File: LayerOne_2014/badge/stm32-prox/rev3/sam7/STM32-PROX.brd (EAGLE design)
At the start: 99 x 50 mm, 273 parts, among them IC10 74XX244, IC105 MCP1824T-250, IC106 MCP1824T-120, IC11 CD4066, IC12 AT91SAM7S64, IC13 PQ1X331M2ZP-3V3-LDO-SOT-23-5, IC14 AD8052, IC3 PQ1X331M2ZP-3V3-LDO-SOT-23-5, IC4 HCU-INVERTER, IC5 TLV3502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

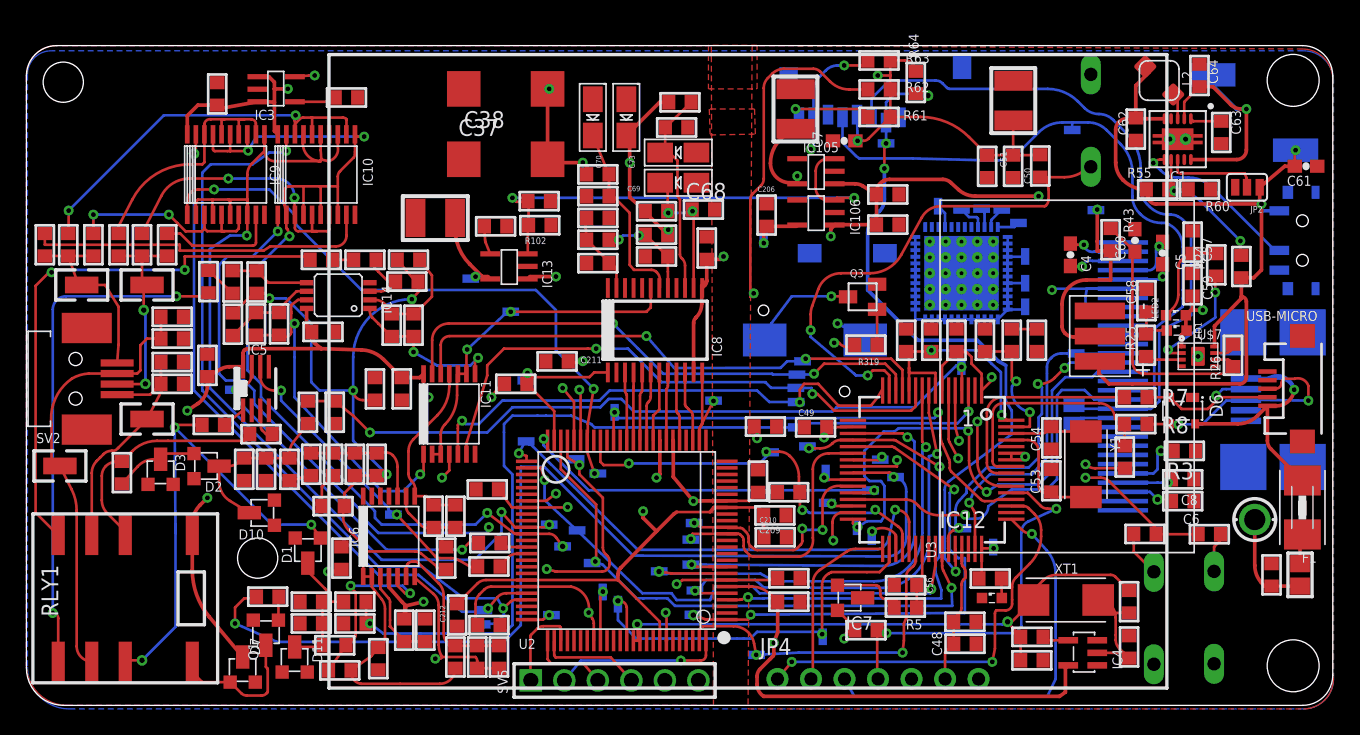
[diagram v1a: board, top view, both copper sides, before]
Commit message: speaker changed.
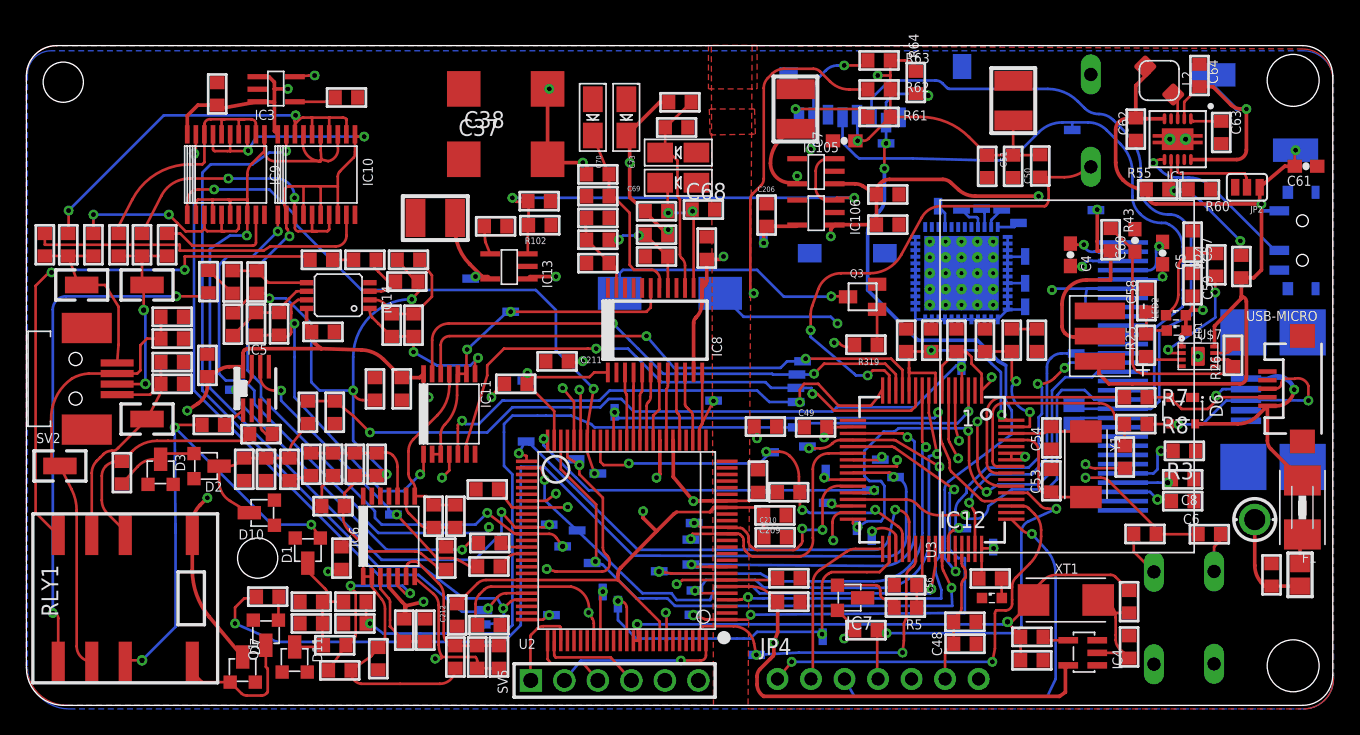
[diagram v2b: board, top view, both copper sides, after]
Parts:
- moved BUZ1 11.5 mm to (48.8, 30.2)
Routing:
- net N$59: track 8.21 -> 19.8 mm
- net +3V3: track 243.6 -> 251.0 mm
- added copper zone on layer 2, net GND
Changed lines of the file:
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@@
 <setting verticaltext="up"/>
 </settings>
-<grid distance="10" unitdist="mil" unit="mil" style="dots" multiple="1" display="yes" altdistance="0.0025" altunitdist="inch" altunit="inch"/>
+<grid distance="1" unitdist="mm" unit="mm" style="dots" multiple="1" display="yes" altdistance="0.1" altunitdist="mm" altunit="mm"/>
 <layers>
 <layer number="1" name="Top" color="4" fill="1" visible="yes" active="yes"/>
@@
 <layer number="19" name="Unrouted" color="6" fill="1" visible="yes" active="yes"/>
 <layer number="20" name="Dimension" color="15" fill="1" visible="yes" active="yes"/>
-<layer number="21" name="tPlace" color="7" fill="1" visible="yes" active="yes"/>
-<layer number="22" name="bPlace" color="7" fill="1" visible="yes" active="yes"/>
+<layer number="21" name="tPlace" color="7" fill="1" visible="no" active="yes"/>
+<layer number="22" name="bPlace" color="7" fill="1" visible="no" active="yes"/>
 <layer number="23" name="tOrigins" color="15" fill="1" visible="yes" active="yes"/>
 <layer number="24" name="bOrigins" color="15" fill="1" visible="yes" active="yes"/>
@@
 <layer number="43" name="vRestrict" color="2" fill="10" visible="no" active="yes"/>
 <layer number="44" name="Drills" color="7" fill="1" visible="no" active="yes"/>
-<layer number="45" name="Holes" color="7" fill="1" visible="yes" active="yes"/>
+<layer number="45" name="Holes" color="7" fill="1" visible="no" active="yes"/>
 <layer number="46" name="Milling" color="3" fill="1" visible="no" active="yes"/>
 <layer number="47" name="Measures" color="7" fill="1" visible="no" active="yes"/>
@@
 <wire x1="2.832684375" y1="-1" x2="96.714" y2="-1" width="0" layer="20"/>
 <wire x1="96.714" y1="-1" x2="99" y2="1.286" width="0" layer="20" curve="90"/>
-<text x="6.46551875" y="33.95144375" size="1.778" layer="52" rot="MR270">www.layerone.org</text>
-<text x="2.6445125" y="35.153565625" size="1.778" layer="52" rot="MR270">LayerOne 2014</text>
+<text x="7.46551875" y="32.95144375" size="1.778" layer="52" rot="MR270">www.layerone.org</text>
+<text x="2.6445125" y="31.153565625" size="1.778" layer="52" rot="MR270">LayerOne 2014</text>
 <text x="23.161175" y="2.4405875" size="1.778" layer="52" rot="MR180">charliex</text>
 <text x="13.843" y="40.64" size="1.778" layer="52" rot="MR270">[ NULL SPACE LABS ]</text>
@@
 arko
 krs</text>
-<text x="48.514" y="41.656" size="1.778" layer="52" rot="MR270">Ten Year Anniversary</text>
+<text x="30.514" y="41.656" size="1.778" layer="52" rot="MR270">Ten Year Anniversary</text>
 <wire x1="74.12868125" y1="-0.2264875" x2="74.12868125" y2="-0.2076125" width="0.4064" layer="52"/>
 <wire x1="77.93868125" y1="-0.2264875" x2="77.93868125" y2="-0.2076125" width="0.4064" layer="52"/>
@@
 <element name="SV1" library="STM32-PROX" package="USB-MINIB-SMD" value="USB-MINIB" x="94.4245" y="23.368" smashed="yes" rot="MR0">
 <attribute name="PARTNO" value="*" x="94.4245" y="23.368" size="1.778" layer="28" rot="MR0" display="off"/>
-<attribute name="NAME" x="88.73055625" y="16.3388" size="1.27" layer="22" ratio="18" rot="MR90"/>
+<attribute name="NAME" x="97.7072" y="13.54655625" size="1.27" layer="22" ratio="18" rot="MR0"/>
 <attribute name="OC_NEWARK" value="unknown" x="94.4245" y="23.368" size="1.778" layer="28" rot="MR0" display="off"/>
 <attribute name="MF" value="" x="94.4245" y="23.368" size="1.778" layer="28" rot="MR0" display="off"/>
@@
 <element name="K3" library="STM32-PROX" package="B3F-5XX" value="" x="90.037" y="5.651" smashed="yes" rot="MR90">
 <attribute name="PARTNO" value="PTS635SL50 LFS" x="90.037" y="5.651" size="1.778" layer="28" rot="MR90" display="off"/>
-<attribute name="NAME" x="92.346903125" y="7.8504125" size="1.27" layer="26" ratio="10" rot="MR90"/>
+<attribute name="NAME" x="92.346903125" y="1.5004125" size="1.27" layer="26" ratio="10" rot="MR90"/>
 <attribute name="VALUE" x="86.457" y="2.603" size="1.27" layer="28" ratio="10" rot="MR90"/>
 <attribute name="OC_NEWARK" value="unknown" x="90.037" y="5.651" size="1.778" layer="28" rot="MR90" display="off"/>
@@
 <attribute name="DIGIKEY" value="MICROSMD050FCT-ND" x="96.7" y="14" size="1.778" layer="27" rot="R90" display="off"/>
 </element>
-<element name="BUZ1" library="STM32-PROX" package="BUZZER" value="BUZZER" x="59.76" y="26.69" smashed="yes" rot="MR180">
-<attribute name="NAME" x="61.30225625" y="34.58605625" size="0.8128" layer="26" ratio="10" rot="MR0"/>
-<attribute name="VALUE" x="61.36" y="31.79" size="0.8128" layer="28" ratio="10" rot="MR270"/>
-<attribute name="PARTNO" value="CCV-084B16" x="59.76" y="26.69" size="1.778" layer="28" rot="MR180" display="off"/>
-<attribute name="OC_NEWARK" value="unknown" x="59.76" y="26.69" size="1.778" layer="28" rot="MR180" display="off"/>
-<attribute name="MF" value="CCV-084B16" x="59.76" y="26.69" size="1.778" layer="28" rot="MR180" display="off"/>
-<attribute name="MPN" value="CCV-084B16" x="59.76" y="26.69" size="1.778" layer="28" rot="MR180" display="off"/>
-<attribute name="DIGIKEY" value="102-1265-1-ND" x="59.76" y="26.69" size="1.778" layer="28" rot="MR180" display="off"/>
-</element>
 <element name="R319" library="STM32-PROX" package="RLC_0603" value="100" x="63.623" y="26.336" smashed="yes" rot="R180">
 <attribute name="NAME" x="64.629684375" y="25.291021875" size="0.5" layer="25" font="vector" rot="R180"/>
@@
 <element name="TP44" library="STM32-PROX" package="SMD-TESTPOINT" value="TESTPAD" x="75.692" y="30.988" rot="MR90"/>
 <element name="TP56" library="STM32-PROX" package="SMD-TESTPOINT" value="TESTPAD" x="75.692" y="33.02" rot="MR90"/>
+<element name="BUZ1" library="STM32-PROX" package="BUZZER" value="BUZZER" x="48.768" y="30.226" rot="MR180"/>
 </elements>
 <signals>
@@
 <contactref element="U40" pad="2"/>
 <contactref element="U40" pad="3"/>
+<polygon width="0.4064" layer="2">
+<vertex x="0" y="48.768"/>
+<vertex x="99.06" y="48.768"/>
+<vertex x="99.06" y="-1.524"/>
+<vertex x="0" y="-1.524"/>
+</polygon>
 <wire x1="91.611" y1="38.263" x2="97.825" y2="39.859" width="0" layer="19" extent="1-1"/>
 <wire x1="89.75" y1="38.1" x2="91.611" y2="38.263" width="0" layer="19" extent="1-1"/>
@@
 <signal name="N$59">
 <contactref element="Q3" pad="3"/>
-<contactref element="BUZ1" pad="2"/>
-<wire x1="55.95" y1="26.69" x2="56.458" y2="27.95" width="0.2032" layer="16"/>
-<wire x1="56.458" y1="27.95" x2="58" y2="30" width="0.2032" layer="16"/>
-<wire x1="58" y1="30" x2="61" y2="30" width="0.2032" layer="16"/>
 <via x="61" y="30" extent="1-16" drill="0.3556"/>
 <wire x1="61" y1="30" x2="62.232" y2="30" width="0.2032" layer="1"/>
 <wire x1="62.232" y1="30" x2="62.269" y2="29.963" width="0.2032" layer="1"/>
+<contactref element="BUZ1" pad="2"/>
+<wire x1="44.958" y1="30.226" x2="44.958" y2="31.75" width="0.2032" layer="16"/>
+<wire x1="44.958" y1="31.75" x2="45.212" y2="32.004" width="0.2032" layer="16"/>
+<wire x1="45.212" y1="32.004" x2="55.372" y2="32.004" width="0.2032" layer="16"/>
+<wire x1="55.372" y1="32.004" x2="57.404" y2="29.972" width="0.2032" layer="16"/>
+<wire x1="57.404" y1="29.972" x2="60.972" y2="29.972" width="0.2032" layer="16"/>
+<wire x1="60.972" y1="29.972" x2="61" y2="30" width="0.2032" layer="16"/>
 </signal>
 <signal name="N$60">
@@
 <contactref element="C49" pad="1"/>
 <contactref element="C50" pad="1"/>
-<contactref element="BUZ1" pad="1"/>
 <contactref element="U3" pad="6"/>
 <contactref element="U3" pad="9"/>
@@
 <wire x1="71.247" y1="25.781" x2="70.524" y2="25.781" width="0.2032" layer="1"/>
 <wire x1="70.524" y1="25.781" x2="70.485" y2="25.82" width="0.2032" layer="1"/>
-<wire x1="63.57" y1="26.69" x2="63.336" y2="26.924" width="0.2032" layer="16" curve="90"/>
-<wire x1="63.336" y1="26.924" x2="61.468" y2="27.94" width="0.2032" layer="16"/>
 <via x="61.468" y="27.94" extent="3-16" drill="0.3556"/>
 <wire x1="61.468" y1="27.94" x2="70.104" y2="27.94" width="0.2032" layer="3"/>
@@
 <wire x1="60.657" y1="20.017" x2="60.657" y2="20.073" width="0.2032" layer="1"/>
 <wire x1="70.27" y1="5.5635" x2="70.27" y2="5.334" width="0.2032" layer="1"/>
+<contactref element="BUZ1" pad="1"/>
+<wire x1="52.578" y1="30.226" x2="54.356" y2="28.448" width="0.2032" layer="16"/>
+<wire x1="54.356" y1="28.448" x2="60.96" y2="28.448" width="0.2032" layer="16"/>
+<wire x1="60.96" y1="28.448" x2="61.468" y2="27.94" width="0.2032" layer="16"/>
 </signal>
 <signal name="USB_PU">

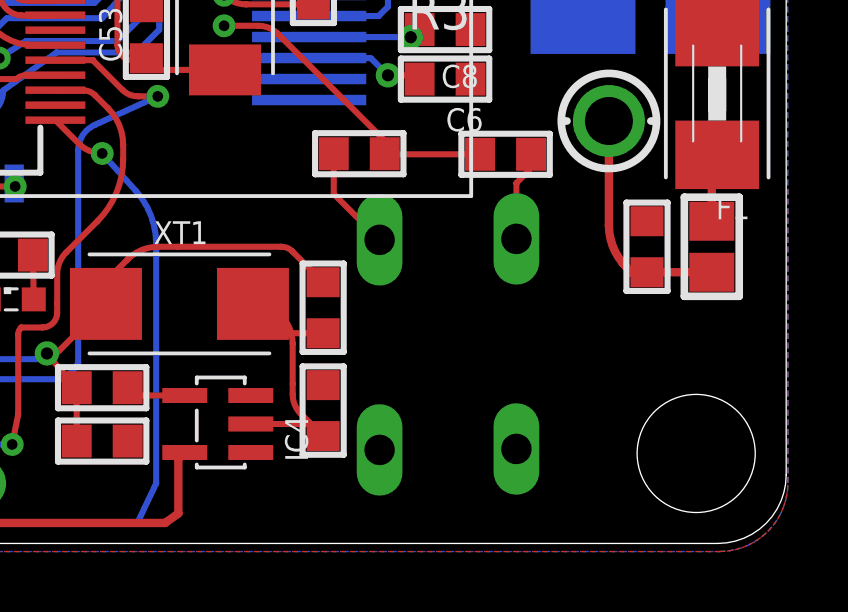
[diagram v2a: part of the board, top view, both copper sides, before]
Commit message: 
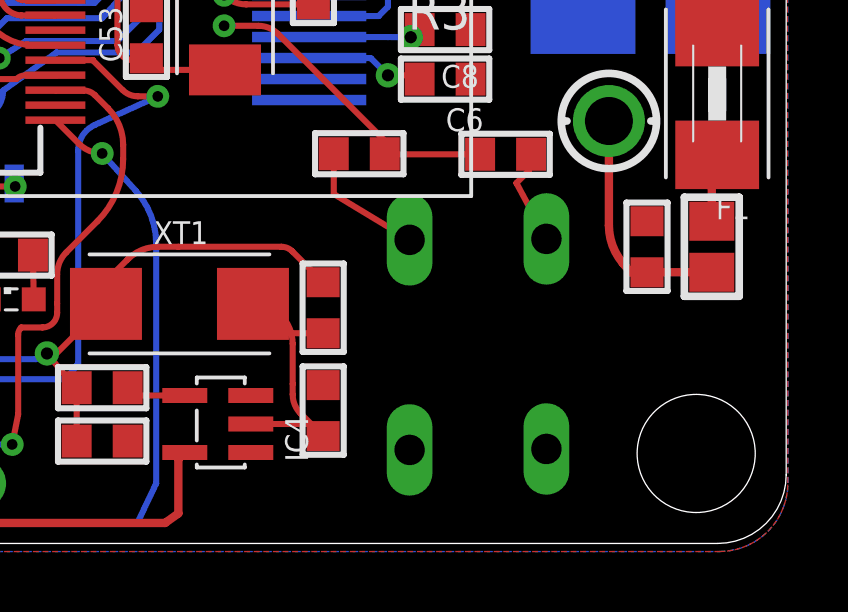
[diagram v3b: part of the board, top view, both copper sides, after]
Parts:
- moved K2 1.00 mm to (86.5, 5.62)
- moved K3 1.00 mm to (91.0, 5.65)
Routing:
- net SW_K2: track 29.1 -> 30.7 mm
- net SW_K3: track 30.5 -> 31.5 mm

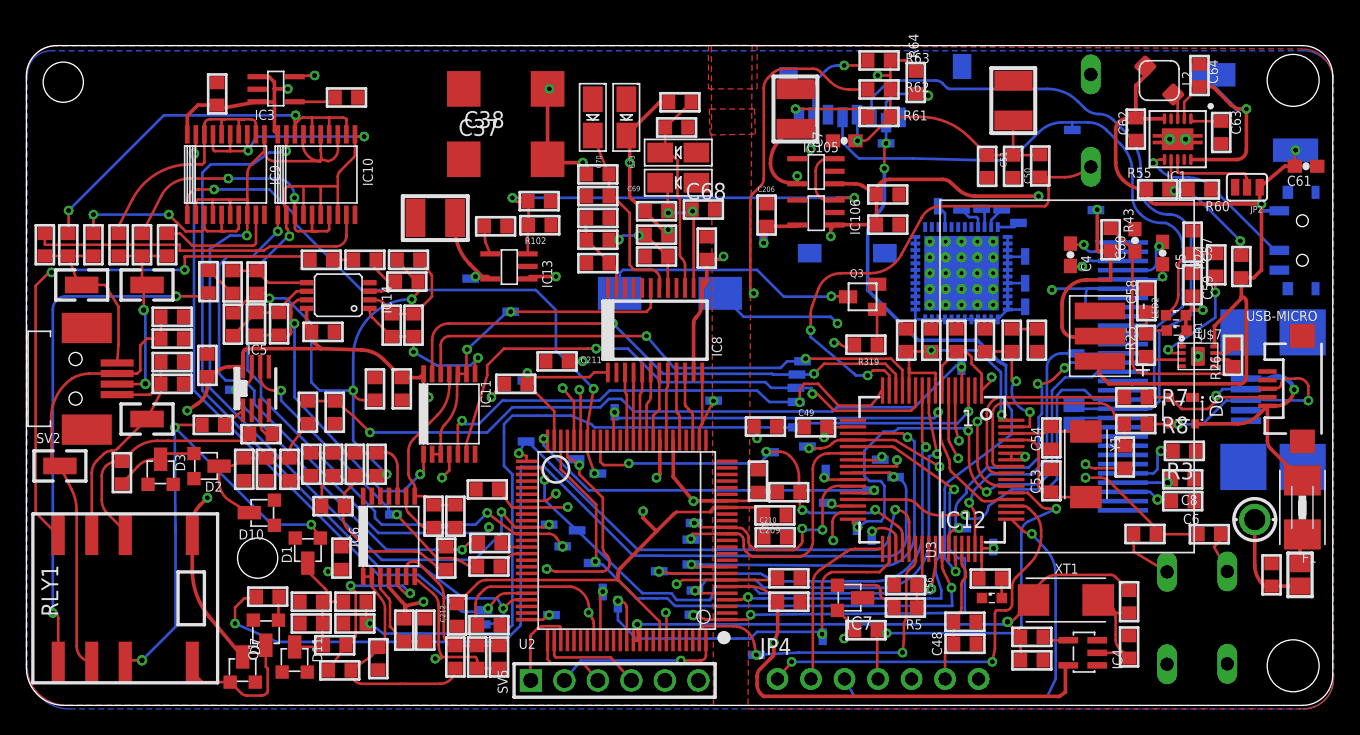
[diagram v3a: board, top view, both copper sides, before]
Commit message: switched on gnds
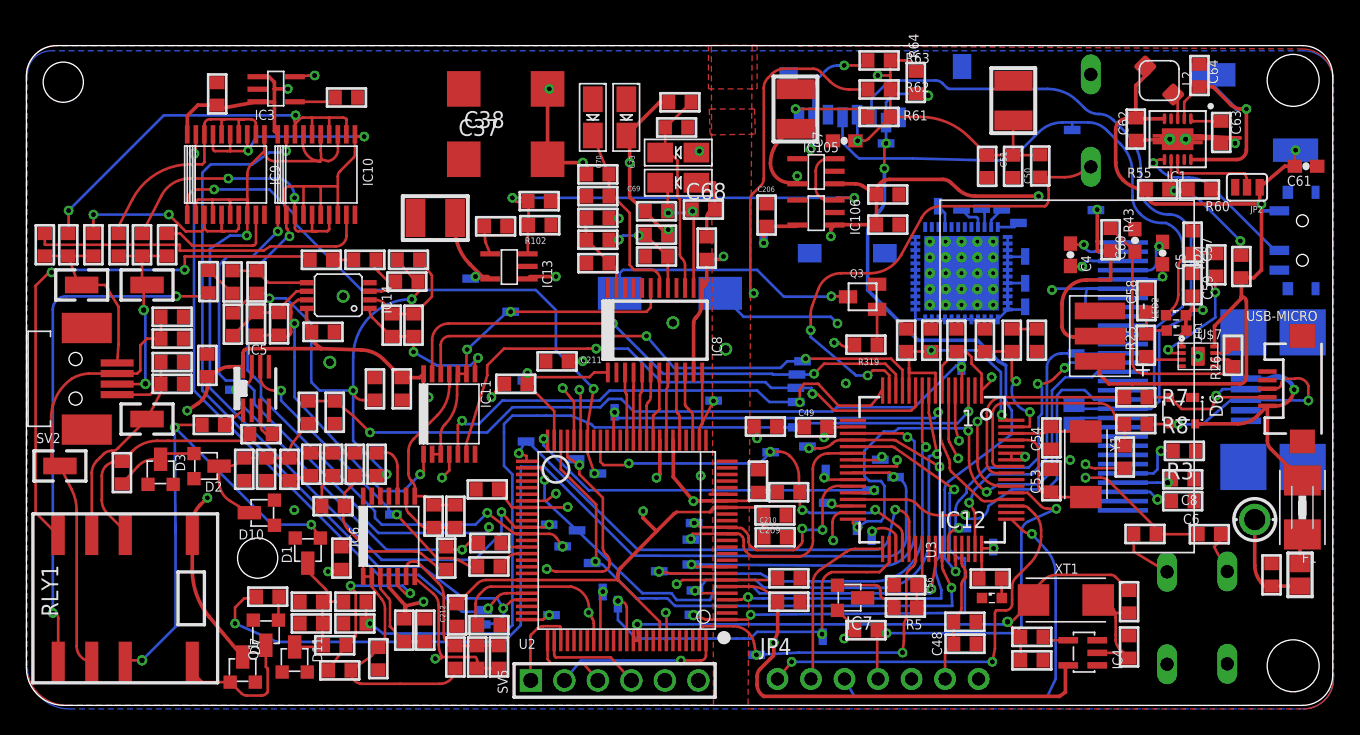
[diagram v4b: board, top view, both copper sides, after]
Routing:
- net GND: track 0.00 -> 17.6 mm, vias 0 -> 11
- net +2V5: track 93.4 -> 92.8 mm
- net FPGA_NINIT: track 31.7 -> 31.1 mm

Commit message: all gnds routed
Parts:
- moved R65 2.06 mm to (74.3, 10.3), turned to 270 degrees
- moved C56 2.03 mm to (66.6, 6.07)
- moved R5 1.40 mm to (66.6, 7.81)
- moved R4 1.02 mm to (63.6, 3.68)
- moved TP53 0.92 mm to (69.9, 24.6), turned to 180 degrees
- moved XT1 0.25 mm to (81.3, 6.99)
- moved C212 0.25 mm to (32.6, 6.10)
- turned R10 to 90 degrees
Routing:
- net GND: track 17.6 -> 52.3 mm, vias 11 -> 54
- net +3V3: track 251.0 -> 254.6 mm
- net SW_K1: track 38.8 -> 40.9 mm
- net N$69: track 5.77 -> 4.39 mm
- net N$76: track 40.5 -> 39.5 mm
- net AMPL_HI: track 55.2 -> 56.2 mm
- net LED3: track 1.48 -> 2.36 mm
- net JTAG_TMS: track 31.8 -> 32.6 mm
- net FPGA_NINIT: track 31.1 -> 31.9 mm
- net N$14: track 7.26 -> 8.00 mm
- net MUXSEL_LOPKD: track 39.4 -> 38.8 mm
- net SW_K3: track 31.5 -> 30.9 mm
- net +2V5: track 92.8 -> 93.3 mm
- net SD_MOSI_DO: track 52.9 -> 52.4 mm
